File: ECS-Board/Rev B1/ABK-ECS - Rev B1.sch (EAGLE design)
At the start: 298 parts, among them J1 USB-B-S-RA, J10 22-05-7028-02, J11 RB1-125BAG1A, J12 22-05-7068-06, J13 22-05-7048-04, J14 22-05-7048-04, J15 22-05-7048-04, J2 MSTBA2, J3 22-05-7068-06, J4 22-05-7068-06, J5 22-05-7068-06, J6 22-05-7068-06, J7 22-05-7028-02, J8 FTSH-103-01-L-DV-NOPASTE, J9 FTSH-105-01-L-DV-NOPASTE, SW1 B3FS-1015, SW2 B3FS-1015, T1 MMBT2907ALT3, T10 MMBT2222AL, T11 IRLML5103TRPBF, T12 MMBT2222AL, T13 IRLML5103TRPBF, T14 IRLML5103TRPBF, T15 IRLML5103TRPBF, T16 IRLML5103TRPBF, T17 MMBT2222AL, T18 MMBT2222AL, T19 MMBT2222AL, T2 EXMACHINA-LOGO-NAME, T20 MMBT2222AL, T3 IRLML5103TRPBF, T4 IRLML5103TRPBF, T5 IRLML5103TRPBF, T6 IRLML5103TRPBF, T7 MMBT2222AL, T8 MMBT2222AL, T9 MMBT2222AL, U1 AT24C512C-SSHM-B, U2 LPC1768FBD100, U3 LT3686HDDPBF, U4 LT3686HDDPBF, U5 CD4050BD, U6 CD4050BD, U7 DP83848JSQ/NOPB, U8 SN74LVC2G17DBVR, U9 SN74LVC2G17DBVR, X1 FC-135, X2 ASE-12, X3 3000, X4 ASE_50

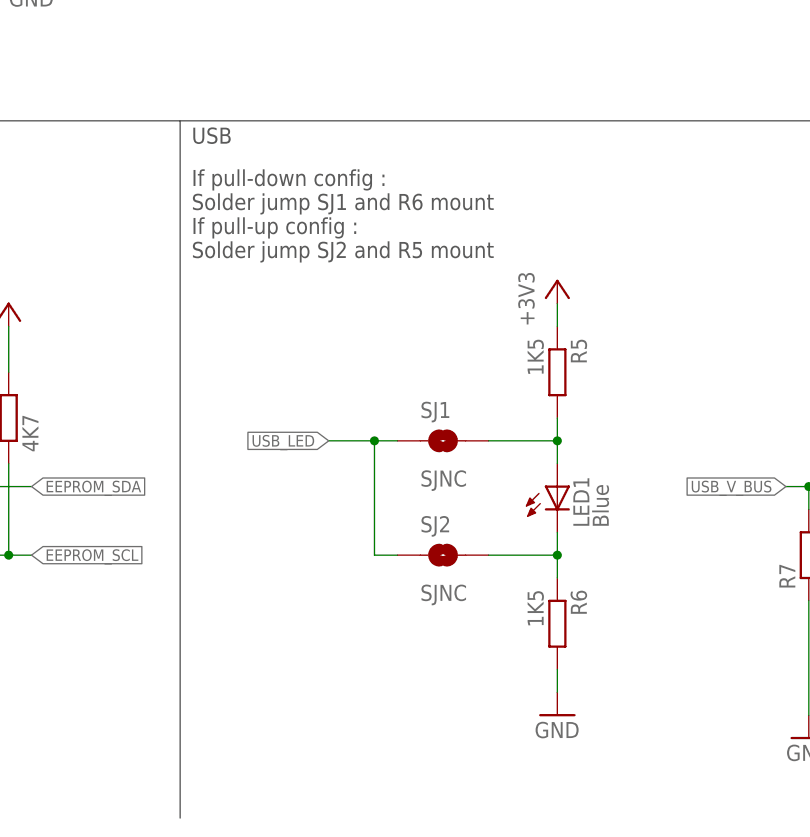
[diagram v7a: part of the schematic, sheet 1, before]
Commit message: Final changes before manufacturing:
- Update silkscreen:
  * Place labels for each pin
  * Update USB silkscreen
  * Update RJ45 silkscreen
  * Update +24V socket silkscreen
  * Update battery holder silscreen
- Remove useless solder jumpers for USB_UP_LED
- Update the guard ring vias
- Enlarge +24V plane
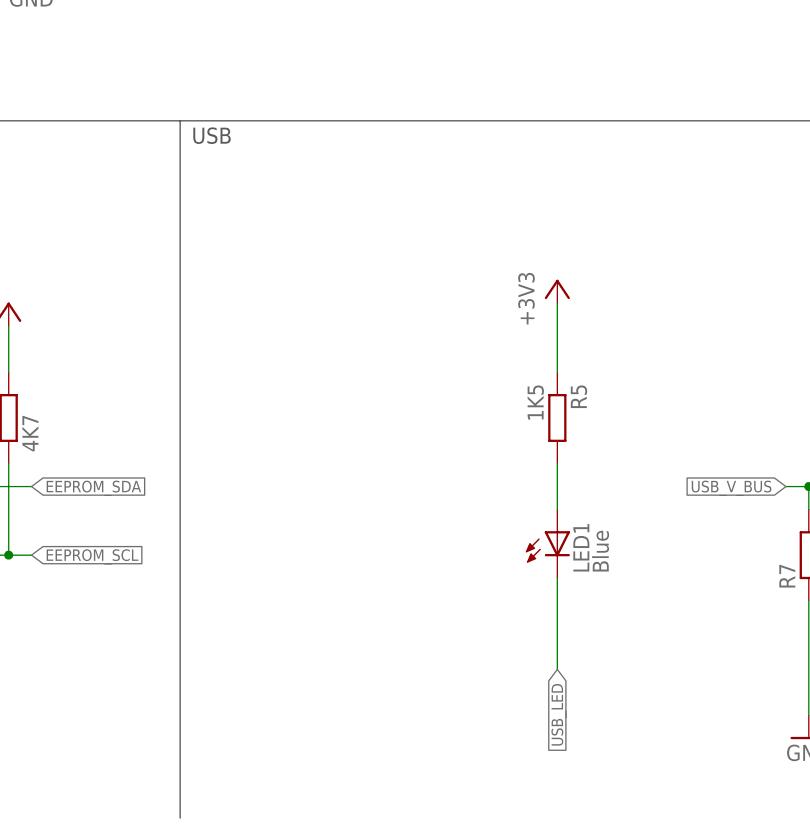
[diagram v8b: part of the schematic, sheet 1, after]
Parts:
- removed R6: 1K5, rcl:R-EU_R0603
- removed SJ1, SJ2: SJNC, SparkFun-Passives:SJNC
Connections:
- removed net N$32: LED1.C, R6.1, SJ2.2
- net GND: no longer R6.2
- net N$28: no longer SJ1.2
- net USB_LED: now also LED1.C; no longer SJ1.1, SJ2.1
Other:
- note removed: "If pull-down config : Solder jump SJ1 and R6 mount If pull-up config : Solder jump SJ2 and R5 mount"
- moved on the sheet: LED1, R5
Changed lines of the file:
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@@
 </variantdefs>
 <classes>
-<class number="0" name="Default" width="0" drill="0">
+<class number="0" name="Default" width="0.1778" drill="0">
 </class>
 <class number="1" name="signal" width="0.1778" drill="0.35">
 </class>
-<class number="2" name="supply" width="0.007740625" drill="0.5">
+<class number="2" name="supply" width="0.4064" drill="0.5">
 </class>
 </classes>
@@
 <attribute name="OC_NEWARK" value="68R0045"/>
 </part>
-<part name="R6" library="rcl" deviceset="R-EU_" device="R0603" value="1K5">
-<attribute name="MF" value=""/>
-<attribute name="MPN" value="RC0603FR-071K5L"/>
-<attribute name="OC_NEWARK" value="68R0045"/>
-</part>
-<part name="GND11" library="supply1" deviceset="GND" device=""/>
 <part name="+3V311" library="supply1" deviceset="+3V3" device=""/>
-<part name="SJ1" library="SparkFun-Passives" deviceset="SJ" device="NC"/>
-<part name="SJ2" library="SparkFun-Passives" deviceset="SJ" device="NC"/>
 </parts>
 <sheets>
@@
 <text x="5.08" y="160.02" size="1.778" layer="97" font="vector">12MHz CLOCK</text>
 <text x="5.08" y="254" size="1.778" layer="97" font="vector">DECOUPLING</text>
-<text x="104.14" y="66.04" size="1.778" layer="97">If pull-down config :
-Solder jump SJ1 and R6 mount
-If pull-up config :
-Solder jump SJ2 and R5 mount</text>
 </plain>
 <instances>
@@
 <attribute name="MPN" x="200.66" y="63.5" size="1.778" layer="96" rot="R90" display="off"/>
 </instance>
-<instance part="LED1" gate="G$1" x="144.78" y="40.64">
-<attribute name="OC_NEWARK" x="144.78" y="40.64" size="1.778" layer="96" display="off"/>
-<attribute name="MF" x="144.78" y="40.64" size="1.778" layer="96" display="off"/>
-<attribute name="MPN" x="144.78" y="40.64" size="1.778" layer="96" display="off"/>
-</instance>
-<instance part="R5" gate="G$1" x="144.78" y="53.34" rot="R270">
-<attribute name="OC_NEWARK" x="144.78" y="53.34" size="1.778" layer="96" display="off"/>
-<attribute name="MF" x="144.78" y="53.34" size="1.778" layer="96" display="off"/>
-<attribute name="MPN" x="144.78" y="53.34" size="1.778" layer="96" display="off"/>
-</instance>
-<instance part="R6" gate="G$1" x="144.78" y="25.4" rot="R270">
-<attribute name="OC_NEWARK" x="144.78" y="25.4" size="1.778" layer="96" display="off"/>
-<attribute name="MF" x="144.78" y="25.4" size="1.778" layer="96" display="off"/>
-<attribute name="MPN" x="144.78" y="25.4" size="1.778" layer="96" display="off"/>
+<instance part="LED1" gate="G$1" x="144.78" y="35.56">
+<attribute name="OC_NEWARK" x="144.78" y="35.56" size="1.778" layer="96" display="off"/>
+<attribute name="MF" x="144.78" y="35.56" size="1.778" layer="96" display="off"/>
+<attribute name="MPN" x="144.78" y="35.56" size="1.778" layer="96" display="off"/>
+</instance>
+<instance part="R5" gate="G$1" x="144.78" y="48.26" rot="R270">
+<attribute name="OC_NEWARK" x="144.78" y="48.26" size="1.778" layer="96" display="off"/>
+<attribute name="MF" x="144.78" y="48.26" size="1.778" layer="96" display="off"/>
+<attribute name="MPN" x="144.78" y="48.26" size="1.778" layer="96" display="off"/>
 </instance>
-<instance part="GND11" gate="1" x="144.78" y="15.24"/>
 <instance part="+3V311" gate="G$1" x="144.78" y="63.5"/>
-<instance part="SJ1" gate="1" x="132.08" y="45.72"/>
-<instance part="SJ2" gate="1" x="132.08" y="33.02"/>
 </instances>
 <busses>
@@
 <pinref part="+3V311" gate="G$1" pin="+3V3"/>
 <pinref part="R5" gate="G$1" pin="1"/>
-<wire x1="144.78" y1="60.96" x2="144.78" y2="58.42" width="0.1524" layer="91"/>
+<wire x1="144.78" y1="60.96" x2="144.78" y2="53.34" width="0.1524" layer="91"/>
 </segment>
 </net>
@@
 <wire x1="172.72" y1="15.24" x2="172.72" y2="27.94" width="0.1524" layer="91"/>
 </segment>
-<segment>
-<pinref part="GND11" gate="1" pin="GND"/>
-<pinref part="R6" gate="G$1" pin="2"/>
-<wire x1="144.78" y1="17.78" x2="144.78" y2="20.32" width="0.1524" layer="91"/>
-</segment>
 </net>
 <net name="JTAG_TDO" class="1">
@@
 </segment>
 <segment>
-<pinref part="SJ2" gate="1" pin="1"/>
-<wire x1="127" y1="33.02" x2="124.46" y2="33.02" width="0.1524" layer="91"/>
-<pinref part="SJ1" gate="1" pin="1"/>
-<wire x1="124.46" y1="33.02" x2="124.46" y2="45.72" width="0.1524" layer="91"/>
-<wire x1="124.46" y1="45.72" x2="127" y2="45.72" width="0.1524" layer="91"/>
-<wire x1="124.46" y1="45.72" x2="119.38" y2="45.72" width="0.1524" layer="91"/>
-<junction x="124.46" y="45.72"/>
-<label x="119.38" y="45.72" size="1.27" layer="95" font="vector" rot="R180" xref="yes"/>
+<wire x1="144.78" y1="30.48" x2="144.78" y2="20.32" width="0.1524" layer="91"/>
+<label x="144.78" y="20.32" size="1.27" layer="95" font="vector" rot="R270" xref="yes"/>
+<pinref part="LED1" gate="G$1" pin="C"/>
 </segment>
 </net>
@@
 <pinref part="R5" gate="G$1" pin="2"/>
 <pinref part="LED1" gate="G$1" pin="A"/>
-<wire x1="144.78" y1="48.26" x2="144.78" y2="45.72" width="0.1524" layer="91"/>
-<pinref part="SJ1" gate="1" pin="2"/>
-<wire x1="144.78" y1="45.72" x2="144.78" y2="43.18" width="0.1524" layer="91"/>
-<wire x1="137.16" y1="45.72" x2="144.78" y2="45.72" width="0.1524" layer="91"/>
-<junction x="144.78" y="45.72"/>
-</segment>
-</net>
-<net name="N$32" class="0">
-<segment>
-<pinref part="LED1" gate="G$1" pin="C"/>
-<pinref part="R6" gate="G$1" pin="1"/>
-<wire x1="144.78" y1="35.56" x2="144.78" y2="33.02" width="0.1524" layer="91"/>
-<pinref part="SJ2" gate="1" pin="2"/>
-<wire x1="144.78" y1="33.02" x2="144.78" y2="30.48" width="0.1524" layer="91"/>
-<wire x1="137.16" y1="33.02" x2="144.78" y2="33.02" width="0.1524" layer="91"/>
-<junction x="144.78" y="33.02"/>
+<wire x1="144.78" y1="43.18" x2="144.78" y2="38.1" width="0.1524" layer="91"/>
 </segment>
 </net>
@@
 <instance part="GND139" gate="1" x="38.1" y="27.94"/>
 <instance part="+3V333" gate="G$1" x="38.1" y="114.3" rot="MR0"/>
-<instance part="+3V334" gate="G$1" x="38.1" y="55.88" rot="MR0"/>
+<instance part="+3V334" gate="G$1" x="38.1" y="63.5" rot="MR0"/>
 <instance part="R141" gate="G$1" x="58.42" y="83.82" rot="R90">
 <attribute name="OC_NEWARK" x="58.42" y="83.82" size="1.778" layer="96" rot="R90" display="off"/>
@@
 <pinref part="+3V334" gate="G$1" pin="+3V3"/>
 <wire x1="33.02" y1="50.8" x2="38.1" y2="50.8" width="0.1524" layer="91"/>
-<wire x1="38.1" y1="50.8" x2="38.1" y2="53.34" width="0.1524" layer="91"/>
+<wire x1="38.1" y1="50.8" x2="38.1" y2="60.96" width="0.1524" layer="91"/>
 </segment>
 <segment>
@@
 </schematic>
 </drawing>
-<compatibility>
-<note version="6.3" minversion="6.2.2" severity="warning">
-Since Version 6.2.2 text objects can contain more than one line,
-which will not be processed correctly with this version.
-</note>
-</compatibility>
 </eagle>
